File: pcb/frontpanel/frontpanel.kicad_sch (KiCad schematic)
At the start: 124 parts, among them J1 PICOBLADE_10POS, J2 CONN_01X03, J3 XILINX_JTAG, J4 DISPLAY, M1 LOGO, M2 LOGO, M3 LOGO, M4 LOGO, Q1 SSM6N58NU, SW1 SWITCH, SW2 SWITCH, U1 STM32L431VxIx, U2 TCA6424A, U3 AT30TS74_UDFN

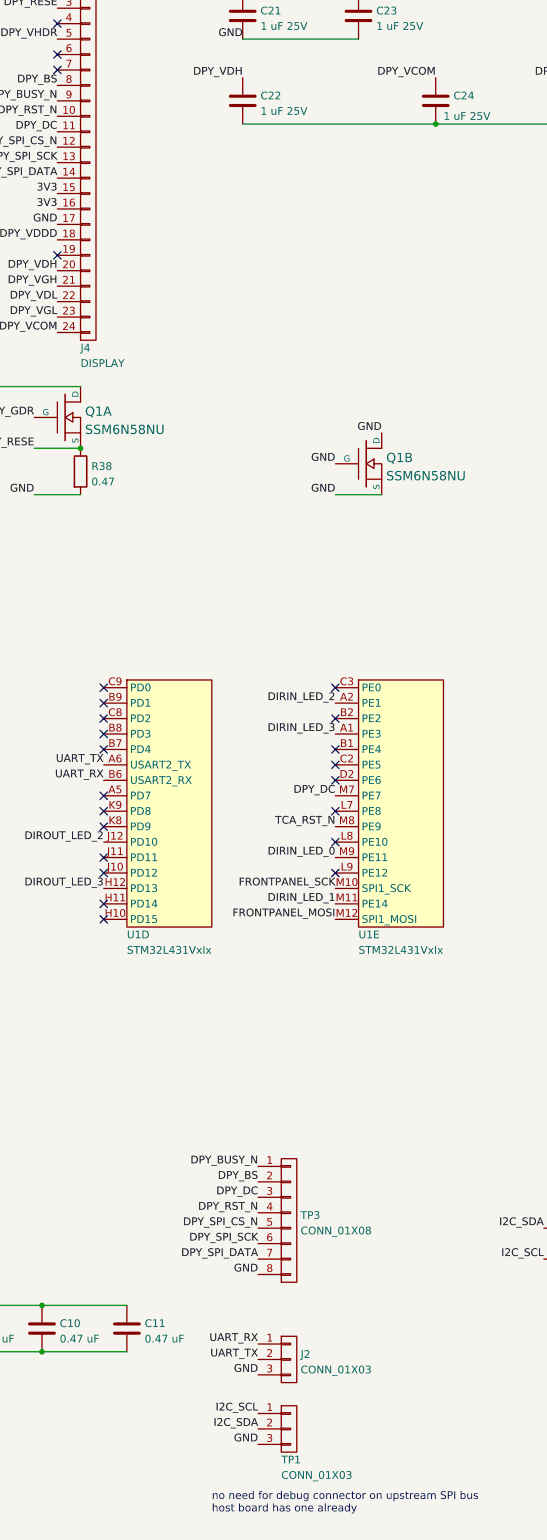
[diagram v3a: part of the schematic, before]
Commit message: Continued front panel PCB layout
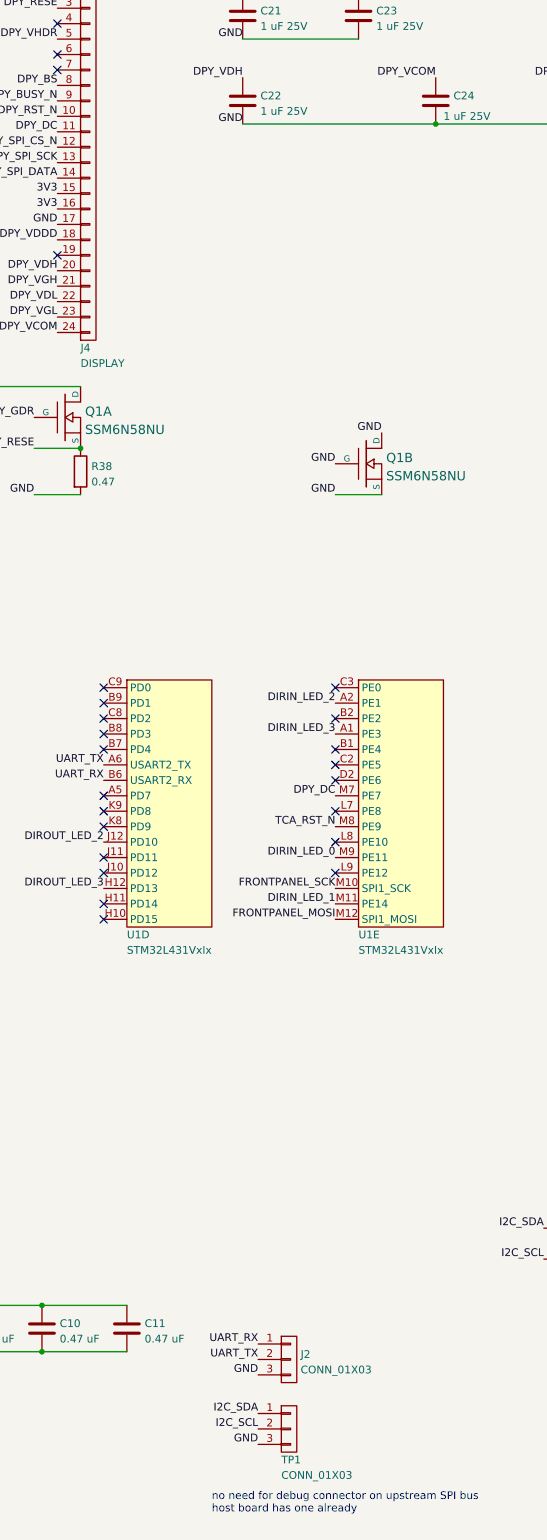
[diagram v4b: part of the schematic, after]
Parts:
- removed TP3: CONN_01X08, azonenberg_pcb:CONN_HEADER_2.54MM_1x8, symbol conn:CONN_01X08
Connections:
- net GND: now also C22.2, C24.2, C25.2
- net I2C_SCL: now also TP1.2 (P2); no longer TP1.1 (P1)
- net I2C_SDA: now also TP1.1 (P1); no longer TP1.2 (P2)
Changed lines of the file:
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@@
     (effects (font (size 1.27 1.27)) (justify right bottom))
   )
-  (label "DPY_SPI_CS_N" (at 168.91 232.41 180)
-    (effects (font (size 1.27 1.27)) (justify right bottom))
-  )
   (label "FRONTPANEL_CS_N" (at 34.925 34.29 0)
     (effects (font (size 1.27 1.27)) (justify left bottom))
@@
     (effects (font (size 1.27 1.27)) (justify right bottom))
   )
-  (label "I2C_SDA" (at 168.91 265.43 180)
+  (label "I2C_SDA" (at 168.91 262.89 180)
     (effects (font (size 1.27 1.27)) (justify right bottom))
   )
@@
     (effects (font (size 1.27 1.27)) (justify right bottom))
   )
+  (label "GND" (at 166.37 50.8 180)
+    (effects (font (size 1.27 1.27)) (justify right bottom))
+  )
   (label "TRIGOUT_LED_5" (at 320.04 71.12 180)
     (effects (font (size 1.27 1.27)) (justify right bottom))
@@
     (effects (font (size 1.27 1.27)) (justify right bottom))
   )
-  (label "DPY_BS" (at 168.91 224.79 180)
-    (effects (font (size 1.27 1.27)) (justify right bottom))
-  )
   (label "GND" (at 264.16 172.72 180)
     (effects (font (size 1.27 1.27)) (justify right bottom))
@@
     (effects (font (size 1.27 1.27)) (justify right bottom))
   )
-  (label "DPY_DC" (at 168.91 227.33 180)
-    (effects (font (size 1.27 1.27)) (justify right bottom))
-  )
   (label "DPY_DC" (at 80.01 31.75 180)
     (effects (font (size 1.27 1.27)) (justify right bottom))
@@
     (effects (font (size 1.27 1.27)) (justify right bottom))
   )
-  (label "GND" (at 168.91 240.03 180)
-    (effects (font (size 1.27 1.27)) (justify right bottom))
-  )
   (label "UART_RX" (at 143.51 158.75 180)
     (effects (font (size 1.27 1.27)) (justify right bottom))
@@
     (effects (font (size 1.27 1.27)) (justify left bottom))
   )
-  (label "DPY_BUSY_N" (at 168.91 222.25 180)
-    (effects (font (size 1.27 1.27)) (justify right bottom))
-  )
-  (label "DPY_SPI_DATA" (at 168.91 237.49 180)
-    (effects (font (size 1.27 1.27)) (justify right bottom))
-  )
   (label "DIROUT_LED_1" (at 106.68 158.75 180)
     (effects (font (size 1.27 1.27)) (justify right bottom))
@@
     (effects (font (size 1.27 1.27)) (justify right bottom))
   )
-  (label "I2C_SCL" (at 168.91 262.89 180)
+  (label "I2C_SCL" (at 168.91 265.43 180)
     (effects (font (size 1.27 1.27)) (justify right bottom))
   )
@@
     (effects (font (size 1.27 1.27)) (justify left bottom))
   )
-  (label "DPY_RST_N" (at 168.91 229.87 180)
-    (effects (font (size 1.27 1.27)) (justify right bottom))
-  )
-  (label "DPY_SPI_SCK" (at 168.91 234.95 180)
-    (effects (font (size 1.27 1.27)) (justify right bottom))
-  )
   (label "TRIGIN_LED_9" (at 364.49 109.22 180)
     (effects (font (size 1.27 1.27)) (justify right bottom))
@@
     )
   )
-  (symbol (lib_id "conn:CONN_01X08") (at 173.99 231.14 0) (unit 1)
-    (in_bom yes) (on_board yes)
-    (property "Reference" "TP3" (id 0) (at 175.895 230.3053 0)
-      (effects (font (size 1.27 1.27)) (justify left))
-    )
-    (property "Value" "CONN_01X08" (id 1) (at 175.895 232.8422 0)
-      (effects (font (size 1.27 1.27)) (justify left))
-    )
-    (property "Footprint" "azonenberg_pcb:CONN_HEADER_2.54MM_1x8" (id 2) (at 173.99 231.14 0)
-      (effects (font (size 1.27 1.27)) hide)
-    )
-    (property "Datasheet" "" (id 3) (at 173.99 231.14 0)
-      (effects (font (size 1.27 1.27)) hide)
-    )
-    (pin "1")
-    (pin "2")
-    (pin "3")
-    (pin "4")
-    (pin "5")
-    (pin "6")
-    (pin "7")
-    (pin "8")
-  )
   (symbol (lib_id "conn:CONN_01X01") (at 370.84 166.37 0) (unit 1)
     (in_bom yes) (on_board yes) (fields_autoplaced)
@@
       (reference "TP2") (unit 1) (value "CONN_01X08") (footprint "azonenberg_pcb:CONN_HEADER_2.54MM_1x8")
     )
-    (path "/78a8c250-c226-4691-9011-31e7be15f9fd"
-      (reference "TP3") (unit 1) (value "CONN_01X08") (footprint "azonenberg_pcb:CONN_HEADER_2.54MM_1x8")
-    )
     (path "/6e410804-fa40-453b-b598-2d4053ae2fdd"

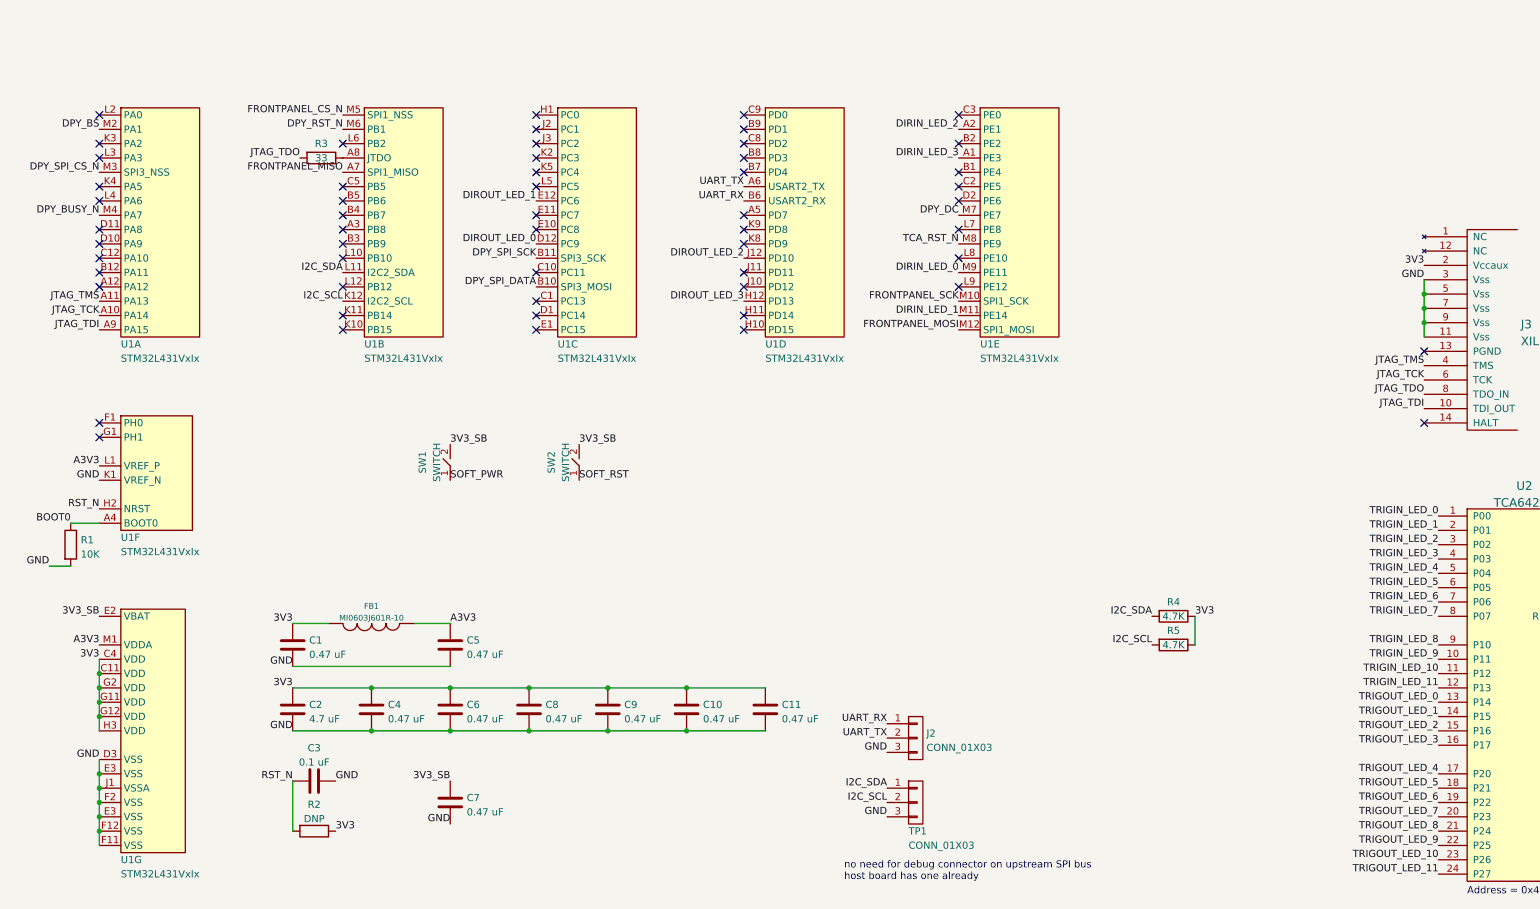
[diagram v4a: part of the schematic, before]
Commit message: Fully routed front panel ready for layout review
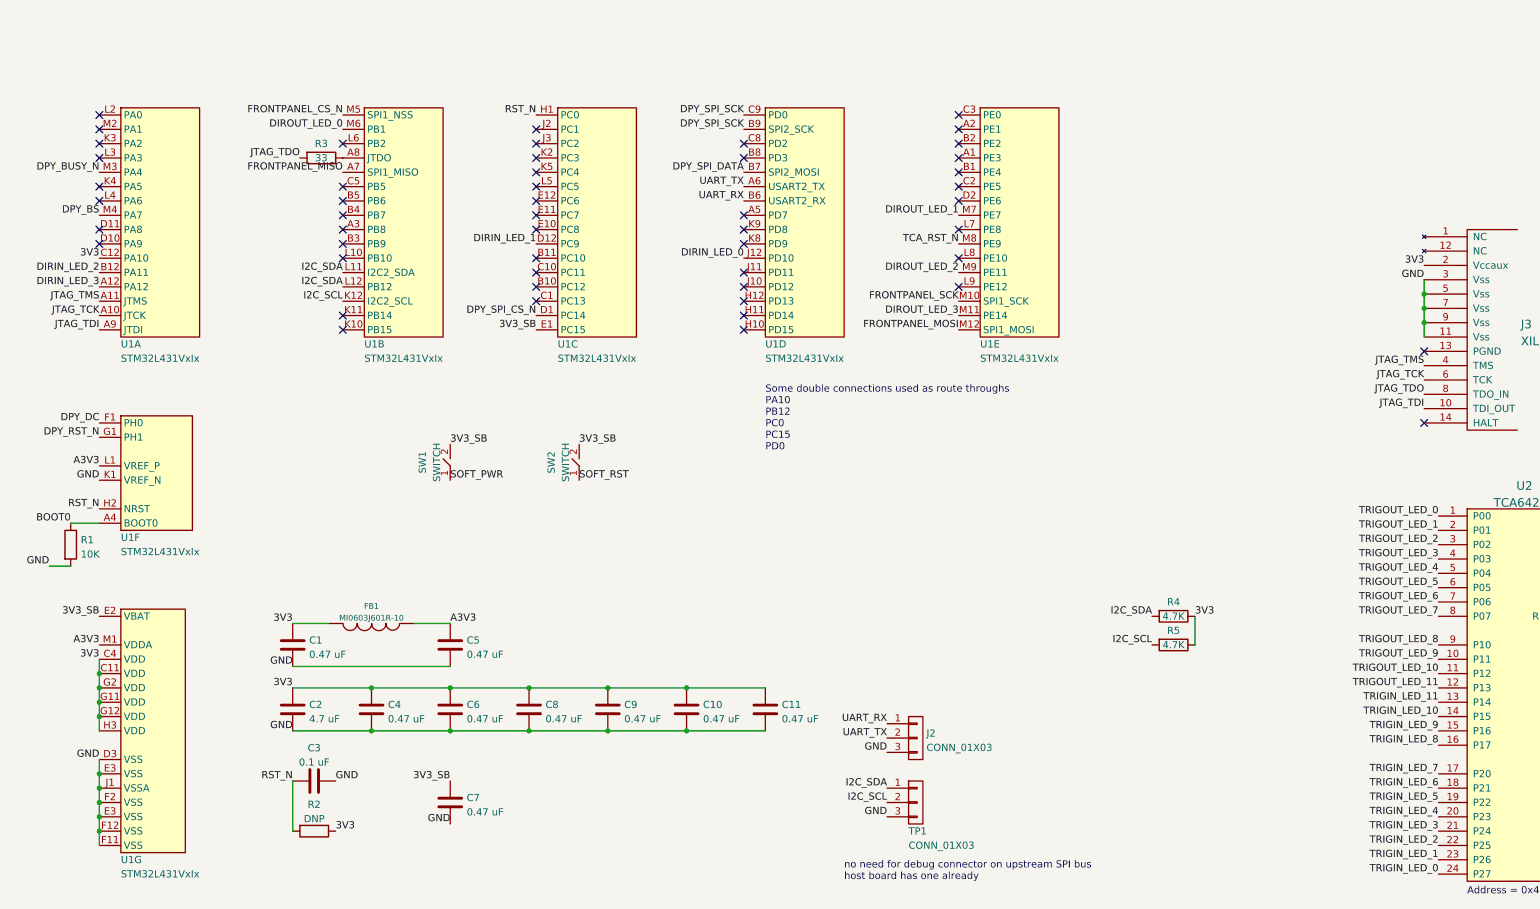
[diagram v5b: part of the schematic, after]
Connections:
- net 3V3: now also U1.C12 (PA10)
- net 3V3_SB: now also U1.E1 (PC15)
- net DIRIN_LED_0: now also U1.J12 (PD10); no longer U1.M9 (PE11)
- net DIRIN_LED_1: now also U1.D12 (PC9); no longer U1.M11 (PE14)
- net DIRIN_LED_2: now also U1.B12 (PA11); no longer U1.A2 (PE1)
- net DIRIN_LED_3: now also U1.A12 (PA12); no longer U1.A1 (PE3)
- net DIROUT_LED_0: now also U1.M6 (PB1); no longer U1.D12 (PC9)
- net DIROUT_LED_1: now also U1.M7 (PE7); no longer U1.E12 (PC6)
- net DIROUT_LED_2: now also U1.M9 (PE11); no longer U1.J12 (PD10)
- net DIROUT_LED_3: now also U1.M11 (PE14); no longer U1.H12 (PD13)
- net DPY_BS: now also U1.M4 (PA7); no longer U1.M2 (PA1)
- net DPY_BUSY_N: now also U1.M3 (PA4); no longer U1.M4 (PA7)
- net DPY_DC: now also U1.F1 (PH0); no longer U1.M7 (PE7)
- net DPY_RST_N: now also U1.G1 (PH1); no longer U1.M6 (PB1)
- net DPY_SPI_CS_N: now also U1.D1 (PC14); no longer U1.M3 (PA4)
- net DPY_SPI_DATA: now also U1.B7 (PD4); no longer U1.B10 (PC12)
- net DPY_SPI_SCK: now also U1.B9 (PD1), U1.C9 (PD0); no longer U1.B11 (PC10)
- net I2C_SDA: now also U1.L12 (PB12)
- net RST_N: now also U1.H1 (PC0)
- net TRIGIN_LED_0: now also U2.24 (P27); no longer U2.1 (P00)
- net TRIGIN_LED_1: now also U2.23 (P26); no longer U2.2 (P01)
- net TRIGIN_LED_10: now also U2.14 (P15); no longer U2.11 (P12)
- net TRIGIN_LED_11: now also U2.13 (P14); no longer U2.12 (P13)
- net TRIGIN_LED_2: now also U2.22 (P25); no longer U2.3 (P02)
- net TRIGIN_LED_3: now also U2.21 (P24); no longer U2.4 (P03)
- net TRIGIN_LED_4: now also U2.20 (P23); no longer U2.5 (P04)
- net TRIGIN_LED_5: now also U2.19 (P22); no longer U2.6 (P05)
- net TRIGIN_LED_6: now also U2.18 (P21); no longer U2.7 (P06)
- net TRIGIN_LED_7: now also U2.17 (P20); no longer U2.8 (P07)
- net TRIGIN_LED_8: now also U2.16 (P17); no longer U2.9 (P10)
- net TRIGIN_LED_9: now also U2.15 (P16); no longer U2.10 (P11)
- net TRIGOUT_LED_0: now also U2.1 (P00); no longer U2.13 (P14)
- net TRIGOUT_LED_1: now also U2.2 (P01); no longer U2.14 (P15)
- net TRIGOUT_LED_10: now also U2.11 (P12); no longer U2.23 (P26)
- net TRIGOUT_LED_11: now also U2.12 (P13); no longer U2.24 (P27)
- net TRIGOUT_LED_2: now also U2.3 (P02); no longer U2.15 (P16)
- net TRIGOUT_LED_3: now also U2.4 (P03); no longer U2.16 (P17)
- net TRIGOUT_LED_4: now also U2.5 (P04); no longer U2.17 (P20)
- net TRIGOUT_LED_5: now also U2.6 (P05); no longer U2.18 (P21)
- net TRIGOUT_LED_6: now also U2.7 (P06); no longer U2.19 (P22)
- net TRIGOUT_LED_7: now also U2.8 (P07); no longer U2.20 (P23)
- net TRIGOUT_LED_8: now also U2.9 (P10); no longer U2.21 (P24)
- net TRIGOUT_LED_9: now also U2.10 (P11); no longer U2.22 (P25)
- no-connect marks 67 -> 62
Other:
- note added: "Some double connections used as route throughs PA10 PB12 PC0 PC15 PD0"

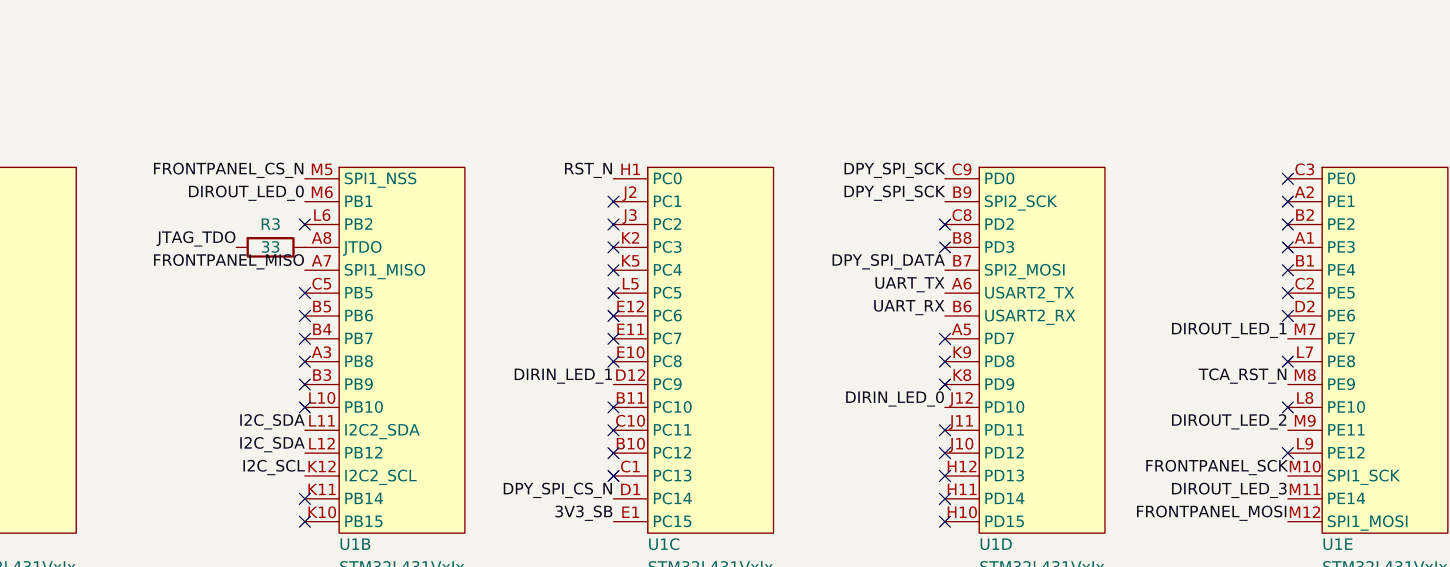
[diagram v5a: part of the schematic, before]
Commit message: Hopefully-final front panel PCB layout after layout review, pending final exports and mechanical fit check on enclosure
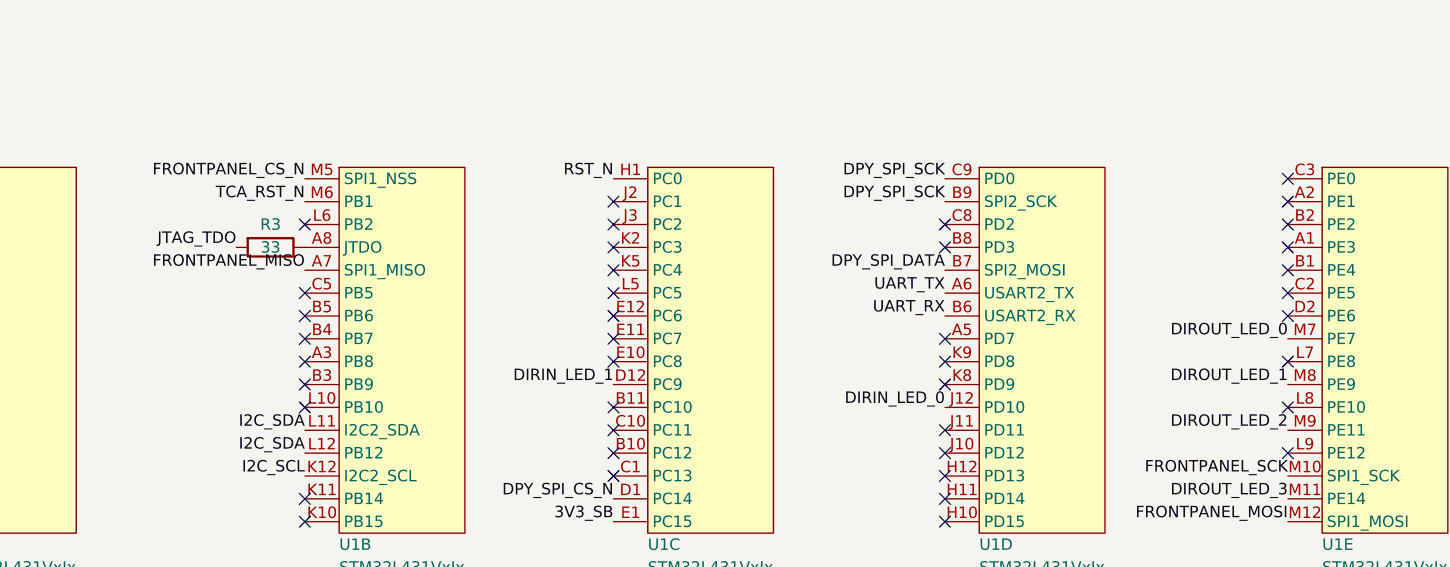
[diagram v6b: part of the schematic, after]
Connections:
- net DIROUT_LED_0: now also U1.M7 (PE7); no longer U1.M6 (PB1)
- net DIROUT_LED_1: now also U1.M8 (PE9); no longer U1.M7 (PE7)
- net TCA_RST_N: now also U1.M6 (PB1); no longer U1.M8 (PE9)
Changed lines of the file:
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@@
     (effects (font (size 1.27 1.27)) (justify right bottom))
   )
-  (label "DIROUT_LED_0" (at 72.39 146.05 180)
+  (label "DIROUT_LED_0" (at 181.61 161.29 180)
     (effects (font (size 1.27 1.27)) (justify right bottom))
   )
@@
     (effects (font (size 1.27 1.27)) (justify right bottom))
   )
-  (label "TCA_RST_N" (at 181.61 166.37 180)
+  (label "TCA_RST_N" (at 72.39 146.05 180)
     (effects (font (size 1.27 1.27)) (justify right bottom))
   )
@@
     (effects (font (size 1.27 1.27)) (justify left bottom))
   )
-  (label "DIROUT_LED_1" (at 181.61 161.29 180)
+  (label "DIROUT_LED_1" (at 181.61 166.37 180)
     (effects (font (size 1.27 1.27)) (justify right bottom))
   )
